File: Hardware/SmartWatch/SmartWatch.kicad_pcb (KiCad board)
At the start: 6 copper layers, 38.1 x 38.1 mm, 78 parts, among them IC1 6PAIC3109TWRHMRQ1, IC2 SPG08P4HM4H-1, IC3 MC3630, J1 Charging Port, J2 DA_PROG_CONN, J3 ARD_PROG_CONN, J4 Adafruit 4520, M1 c0720b001f, Q1 ECH8693R-TL-W, Q2 ECH8693R-TL-W, SW1 SW_MEC_5E, SW2 SW_MEC_5E, SW3 SW_MEC_5E, U1 BQ297xy, U2 ATmega328P-MMH, U3 W25Q128JVS, U4 MAX30100EFD+, U5 DA14683-00000A92, Y1 16Mhz, Y2 16Mhz, Y3 32.768Mhz

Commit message: [Update] Added communication with codec.
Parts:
- SW1: value SW_MEC_5E -> UP
- SW2: value SW_MEC_5E -> CHOOSE
- SW3: value SW_MEC_5E -> DOWN
- moved L1 90.5 mm to (118.4, 77.5), turned to 90 degrees
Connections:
- L1 pad 2: /LA -> /LY
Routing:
- net +3V3: track 0.00 -> 10.0 mm, vias 0 -> 2
- net GND: track 52.7 -> 57.3 mm, vias 0 -> 1
- net /LX: track 0.00 -> 4.01 mm
- net Net-(AE1-Pad1): track 5.86 -> 9.69 mm
- net /RFIOP: track 29.9 -> 29.0 mm
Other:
- net class Default: clearance 0.2 -> 0.127; trace_width 0.25 -> 0.127
- rule trace_clearance: 0.2 -> 0.127

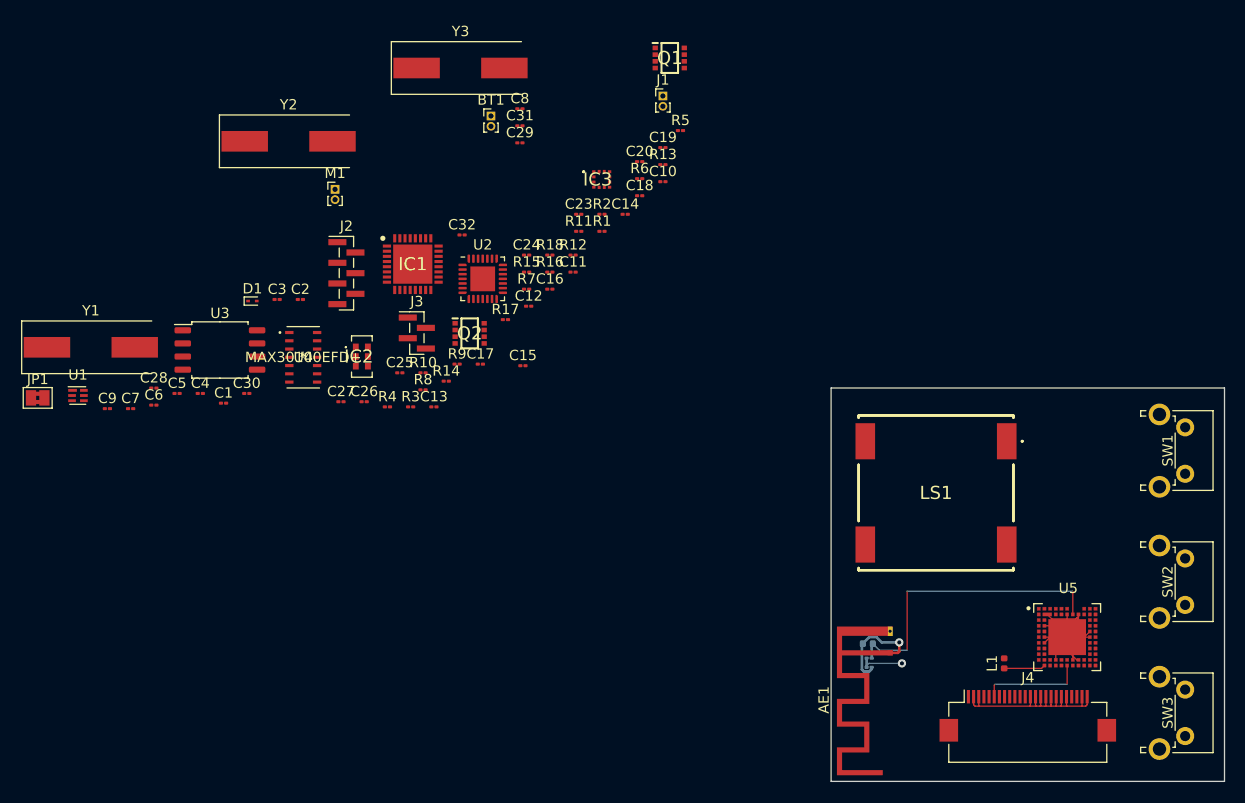
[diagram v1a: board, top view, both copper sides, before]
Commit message: [Update] Added BLE smartphone connection.
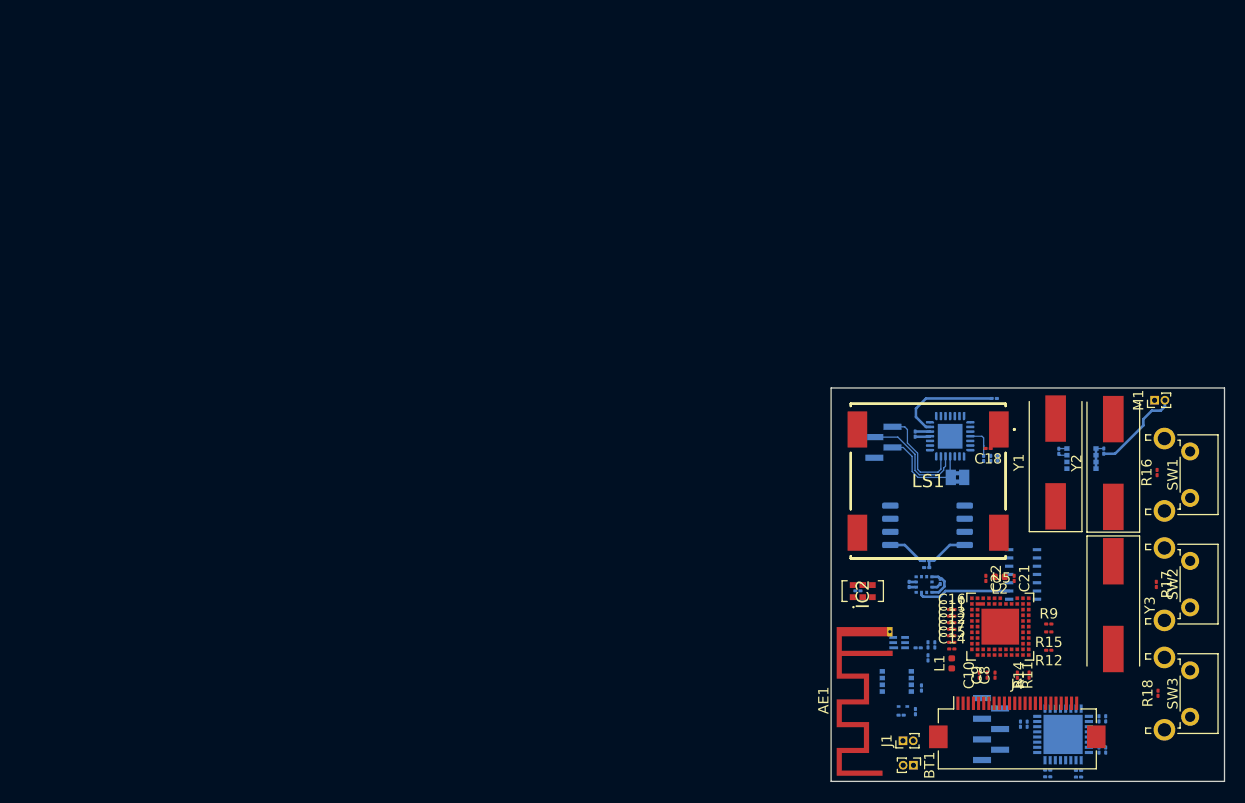
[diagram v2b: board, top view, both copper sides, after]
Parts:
- C1, C19, C2, C20, C23, C24, C25, C26, C27, C28, C29, C3, C30, C31, C32, C4, C5, C6, C7, D1, IC1, IC3, J2, J3, JP1, Q1, Q2, R1, R10, R13, R2, R3, R4, R5, R6, R7, R8, U2: moved to B.Cu
- C21, C22, L2: moved to F.Cu
- U1: value BQ297xy -> BQ29700DSER; moved to B.Cu
- U3: value W25Q128JVS -> W25Q128JVSIQ; moved to B.Cu
- U4: value MAX30100EFD+ -> MAX30100EFD+T; moved to B.Cu
- moved C28 98.0 mm to (127.5, 85.9), turned to 90 degrees
- moved Y1 94.1 mm to (123.3, 58.0), turned to 90 degrees
- moved JP1 89.4 mm to (113.8, 59.5), turned to 180 degrees
- moved C9 89.0 mm to (116.7, 78.6), turned to 90 degrees
- moved C30 88.3 mm to (127.5, 82.8), turned to 90 degrees
- moved Y2 85.7 mm to (128.9, 58.1), turned to 90 degrees
- moved C31 83.1 mm to (125.6, 88.5)
- moved U1 83.1 mm to (108.2, 75.5)
- moved M1 82.0 mm to (132.9, 52.0), turned to 90 degrees
- moved Y3 81.9 mm to (128.9, 71.8), turned to 270 degrees
- moved C27 81.4 mm to (128.2, 85.9), turned to 270 degrees
- moved C29 81.4 mm to (125.6, 87.8), turned to 180 degrees
- moved C7 80.2 mm to (112.2, 69.5), turned to 270 degrees
- moved C5 79.1 mm to (117.4, 51.8), turned to 180 degrees
- moved C32 78.0 mm to (128.2, 82.8), turned to 270 degrees
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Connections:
- IC1 pad 1: Net-(IC1-Pad1) -> /P1_1
- IC1 pad 2: Net-(IC1-Pad2) -> /P1_2
- IC1 pad 3: Net-(IC1-Pad3) -> /P1_7
- IC1 pad 31: Net-(IC1-Pad31) -> /P0_7
- IC1 pad 33: Net-(IC1-Pad33) -> GND
- IC1 pad 4: Net-(IC1-Pad4) -> /P3_1
- IC1 pad 5: Net-(IC1-Pad5) -> /P3_2
- J3 pad 3: /ARD_TX -> /ARD_RX
- J3 pad 4: /ARD_RX -> /ARD_TX
- J4 pad 10: /WR -> /P3_4
- J4 pad 11: /RD -> GND
- SW1 pad 2: Net-(SW1-Pad2) -> /P1_4
- SW2 pad 2: Net-(SW2-Pad2) -> /P1_5
- SW3 pad 2: Net-(SW3-Pad2) -> /P1_6
- U5 pad A7: /P3_3 -> /DC
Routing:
- net GND: track 57.3 -> 6.50 mm, vias 1 -> 0
- net /RFIOP: track 29.0 -> 0.00 mm, vias 3 -> 0
- net /ARD_RX: track 0.00 -> 10.7 mm
- net Net-(C5-Pad2): track 0.00 -> 10.3 mm
- net /ARD_RST: track 0.00 -> 9.77 mm
- net Net-(AE1-Pad1): track 9.69 -> 0.00 mm, vias 1 -> 0
- net /ARD_TX: track 0.00 -> 9.55 mm
- net /P3_7: track 0.00 -> 9.05 mm
- net Net-(M1-Pad2): track 0.00 -> 8.77 mm
- net +3V3: track 10.0 -> 4.74 mm, vias 2 -> 0
- net /LX: track 4.01 -> 0.00 mm
- net Net-(R8-Pad1): track 0.00 -> 3.89 mm
- net +1V8: track 0.00 -> 3.33 mm
- net Net-(Q2-Pad5): track 0.00 -> 2.70 mm
- net Net-(C4-Pad2): track 0.00 -> 1.45 mm
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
